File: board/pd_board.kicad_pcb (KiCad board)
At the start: 2 copper layers, 50 x 50 mm, 9 parts, among them P1 Vin Gnd, P2 OUT 1, P3 OUT 2, P4 OUT 3, P5 OUT 4, P6 OUT 5, P7 OUT 6, P8 OUT 7, P9 OUT 8

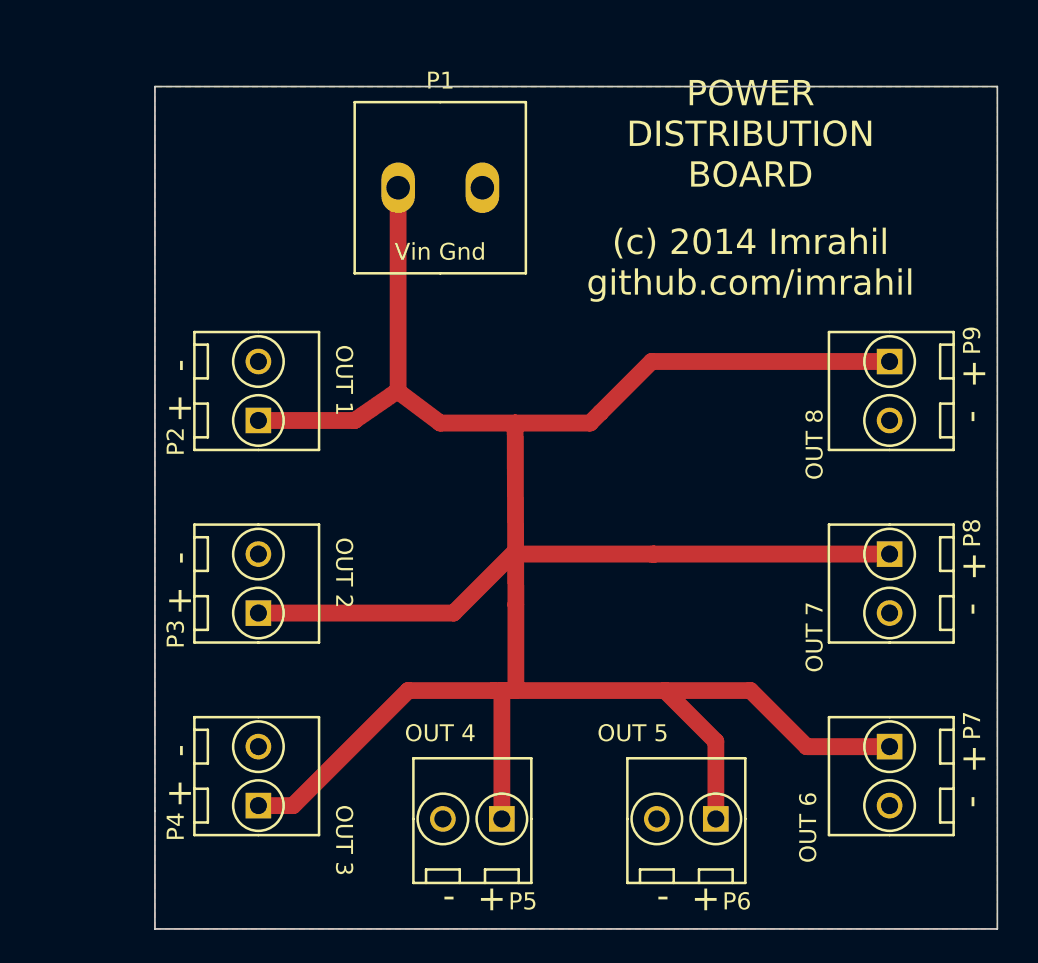
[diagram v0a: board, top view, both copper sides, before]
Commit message: Resized pads, moved tracks to bottom layer
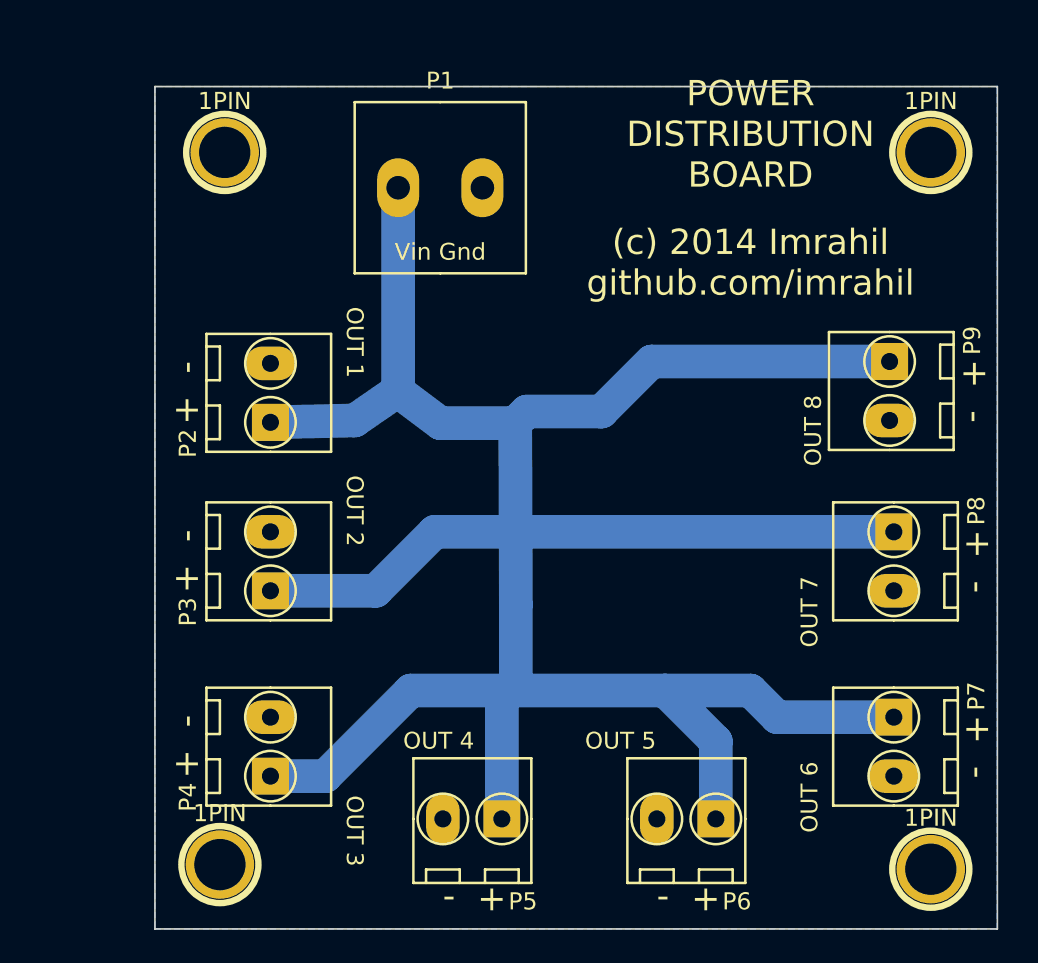
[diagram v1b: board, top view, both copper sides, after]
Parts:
- added 1PIN: P***, 1pin, F.Cu at (121.3, 125.7)
- added 1PIN: P***, 1pin, F.Cu at (163.2, 125.7)
- added 1PIN: P***, 1pin, F.Cu at (163.2, 168.3)
- added 1PIN: P***, 1pin, F.Cu at (121.0, 168.0)
- moved P4 1.89 mm to (124.0, 161.0)
- moved P7 1.77 mm to (161.0, 161.0)
- moved P3 1.50 mm to (124.0, 150.0)
- moved P8 1.34 mm to (161.0, 150.0)
- moved P2 0.72 mm to (124.0, 140.0)
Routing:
- net VCC: track 166.3 -> 163.3 mm
- added copper zone on B.Cu, net GND
- removed copper zone on F.Cu, net GND
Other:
- net class gnd removed
- net class power: trace_width 1 -> 2

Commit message: Cleanup. Minor changes
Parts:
- added G***: OSHW-logo_silkscreen-front_20mm, OSHW-logo_silkscreen-front_20mm, F.Cu at (135.2, 145.3)
- moved P4 8.08 mm to (116.5, 158.0)
- moved P7 8.08 mm to (153.5, 158.0)
- moved P2 7.76 mm to (116.5, 138.0)
- moved P3 7.76 mm to (116.5, 148.0)
- moved P8 7.76 mm to (153.5, 148.0)
- moved P9 7.49 mm to (153.5, 138.0)
- moved 1PIN 7.28 mm to (114.3, 123.7)
- moved 1PIN 7.28 mm to (156.2, 123.7)
- moved 1PIN 7.28 mm to (156.2, 166.3)
- moved 1PIN 7.28 mm to (114.0, 166.0)
- moved P5 7.21 mm to (129.0, 163.5)
- moved P1 7.09 mm to (127.0, 127.5)
- moved P6 6.92 mm to (142.0, 163.5)
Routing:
- added copper zone on F.Cu, net GND
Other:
- outline, holes or cut-outs redrawn
- board text added: "(c) 2014 Imrahil github.com/imrahil/pdb"
- board text added: "VIN GND"
- board text removed: "(c) 2014 Imrahil github.com/imrahil"
